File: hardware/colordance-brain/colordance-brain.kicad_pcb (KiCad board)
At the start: 2 copper layers, 129.5 x 83.5 mm, 118 parts, among them J1 Anderson, J10 RJ45, J11 RJ45, J12 RJ45, J13 RJ45, J14 RJ45, J2 Conn_01x06, J3 Conn_01x03, J4 Conn_01x03, J5 Conn_01x03, J6 Conn_01x03, J7 Conn_01x06, J8 Conn_01x05, J9 RJ45, U1 AP3211, U2 Teensy4.1, U3 AM26LS31x, U4 AM26LS31x, U5 AM26LS31x, U6 74AHCT1G126, U7 74AHCT1G126

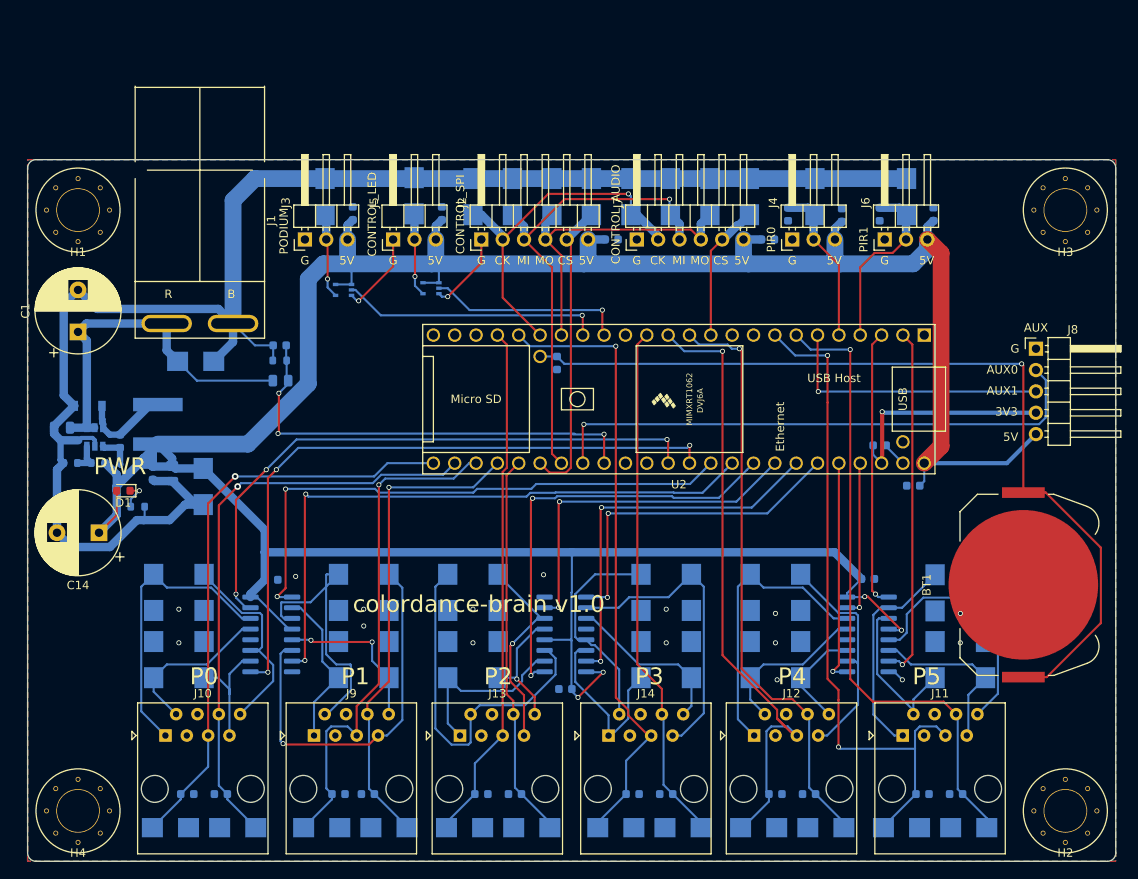
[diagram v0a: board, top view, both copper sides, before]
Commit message: Convert colordance-brain to KiCAD 6
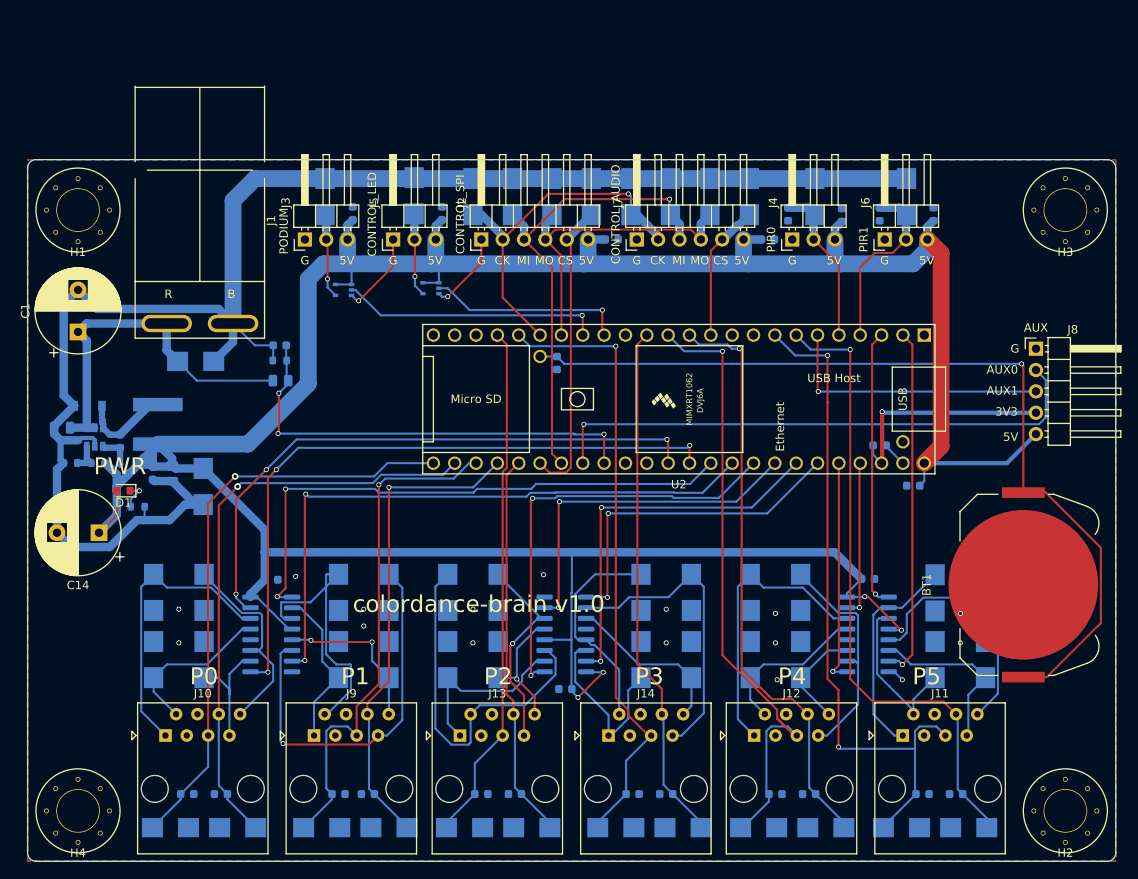
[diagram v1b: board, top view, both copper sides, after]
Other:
- net class Default removed

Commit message: colordance-brain v1.1
- Switch from SPI to serial-over-RS422 for communication with the
interface. Using the Teensy 4.1 as a SPI peripheral did not work. Using
RS422 will allow us to place the interface far away (e.g. 50ft) from the
brain.
- Also break out an extra serial port, e.g. for music playing?
- Change protection for most I/O pins to resistor + cap instead of TVS
diode
- Add a builtin button, for activating test modes
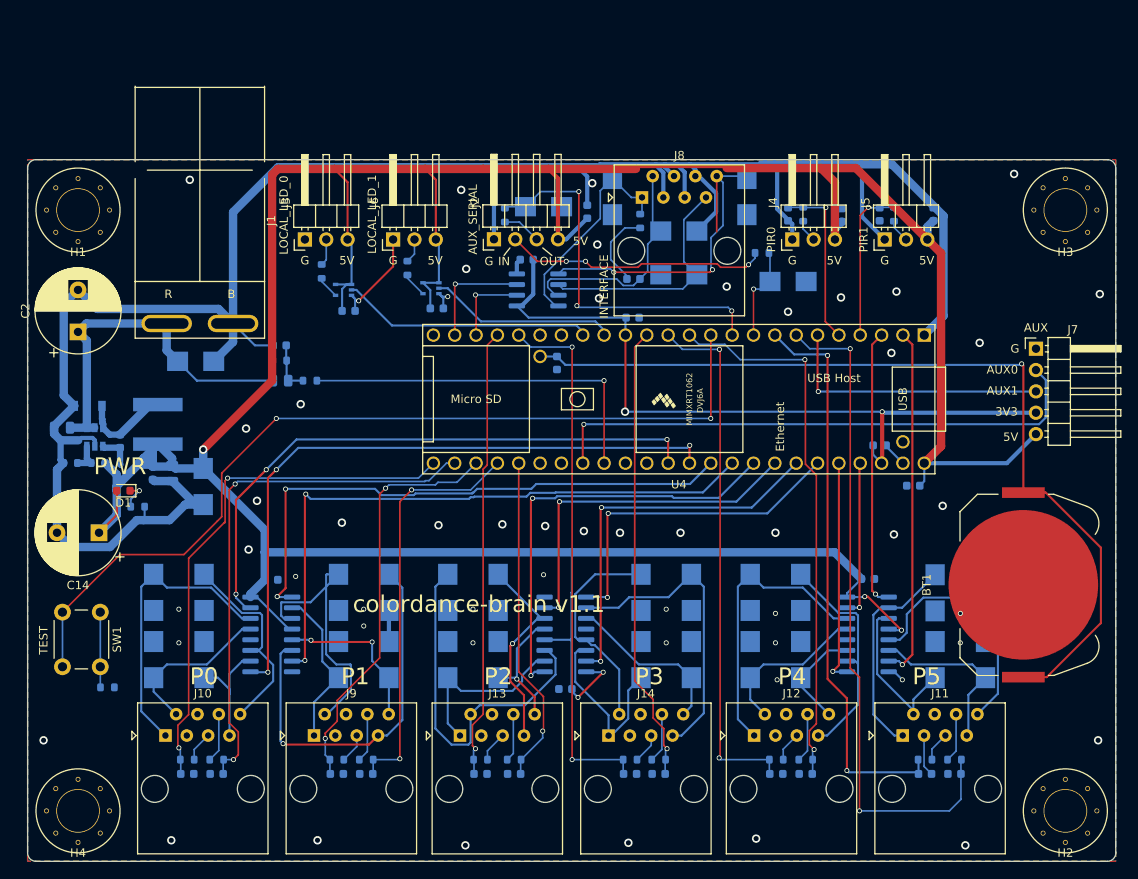
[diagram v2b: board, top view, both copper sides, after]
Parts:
- removed the C13 at (103.1, 56.0)
- removed the C21 at (38.0, 122.0)
- removed the C22 at (34.0, 122.0)
- removed the C26 at (108.0, 122.0)
- removed the C27 at (104.0, 122.0)
- removed the C31 at (91.0, 122.0)
- removed the C32 at (87.0, 122.0)
- removed the C4 at (84.5, 56.0)
- removed the D12 at (119.6, 50.9)
- removed the D13 at (68.0, 50.9)
- removed the D15 at (91.5, 50.9)
- removed the D16 at (77.4, 50.9)
- removed the D17 at (100.9, 50.9)
- removed the D18 at (58.0, 126.0)
- removed the D19 at (50.0, 126.0)
- removed the D24 at (40.0, 126.0)
- removed the D25 at (32.0, 126.0)
- removed the D30 at (127.0, 126.0)
- removed the D31 at (119.0, 126.0)
- removed D36, D37, D42, D43, D48, D49: D_TVS_5V, Diode_SMD:D_SMB
- removed the D5 at (108.7, 50.9)
- removed the D6 at (72.7, 50.9)
- removed the D7 at (96.2, 50.9)
- removed the J7 at (87.5, 56.0)
- added C1: 0.1uF, Capacitor_SMD:C_0603_1608Metric, B.Cu at (81.6, 52.7)
- added C15: 0.1uF, Capacitor_SMD:C_0603_1608Metric, B.Cu at (87.0, 65.3)
- added C19: 0.1uF, Capacitor_SMD:C_0603_1608Metric, B.Cu at (74.4, 58.4)
- added C20: 1300pF, Capacitor_SMD:C_0603_1608Metric, B.Cu at (87.1, 60.7)
- added C24: 22nF, Capacitor_SMD:C_0603_1608Metric, B.Cu at (37.5, 119.6)
- added C25: 22nF, Capacitor_SMD:C_0603_1608Metric, B.Cu at (34.0, 119.6)
- added C29: 22nF, Capacitor_SMD:C_0603_1608Metric, B.Cu at (107.6, 119.6)
- added C30: 22nF, Capacitor_SMD:C_0603_1608Metric, B.Cu at (104.1, 119.6)
- added C34: 22nF, Capacitor_SMD:C_0603_1608Metric, B.Cu at (90.1, 119.6)
- added C35: 22nF, Capacitor_SMD:C_0603_1608Metric, B.Cu at (86.7, 119.6)
- added D11: D_TVS_DATA, Diode_SMD:D_SMB, B.Cu at (100.6, 50.9)
- added D9: D_TVS_DATA, Diode_SMD:D_SMB, B.Cu at (92.5, 55.0)
- added J8: RJ45, Connector_RJ:RJ45_Amphenol_54602-x08_Horizontal, F.Cu at (88.1, 51.0)
- added R12: 1k, Resistor_SMD:R_0603_1608Metric, B.Cu at (118.1, 53.0)
- added R13: 100, Resistor_SMD:R_0603_1608Metric, B.Cu at (60.2, 59.4)
- added R14: 120, Resistor_SMD:R_0603_1608Metric, B.Cu at (87.9, 53.8)
- added R15: 1k, Resistor_SMD:R_0603_1608Metric, B.Cu at (55.3, 117.9)
- added R16: 1k, Resistor_SMD:R_0603_1608Metric, B.Cu at (51.8, 117.9)
- added R17: 1k, Resistor_SMD:R_0603_1608Metric, B.Cu at (37.5, 117.9)
- added R18: 1k, Resistor_SMD:R_0603_1608Metric, B.Cu at (34.0, 117.9)
- added R19: 1k, Resistor_SMD:R_0603_1608Metric, B.Cu at (125.3, 117.9)
- added R20: 1k, Resistor_SMD:R_0603_1608Metric, B.Cu at (121.8, 117.9)
- added R21: 1k, Resistor_SMD:R_0603_1608Metric, B.Cu at (107.6, 117.9)
- added R22: 1k, Resistor_SMD:R_0603_1608Metric, B.Cu at (104.1, 117.9)
- added R23: 1k, Resistor_SMD:R_0603_1608Metric, B.Cu at (72.9, 117.9)
- added R24: 1k, Resistor_SMD:R_0603_1608Metric, B.Cu at (68.9, 117.9)
- added R25: 1k, Resistor_SMD:R_0603_1608Metric, B.Cu at (90.1, 117.9)
- added R26: 1k, Resistor_SMD:R_0603_1608Metric, B.Cu at (86.7, 117.9)
- added R4: 100, Resistor_SMD:R_0603_1608Metric, B.Cu at (102.4, 57.6)
- added R5: 100, Resistor_SMD:R_0603_1608Metric, B.Cu at (50.0, 59.8)
- added R6: 1k, Resistor_SMD:R_0603_1608Metric, B.Cu at (107.3, 53.0)
- added R7: 1k, Resistor_SMD:R_0603_1608Metric, B.Cu at (48.6, 72.8)
- added R8: 100, Resistor_SMD:R_0603_1608Metric, B.Cu at (71.8, 53.1)
- added R9: 1k, Resistor_SMD:R_0603_1608Metric, B.Cu at (24.5, 109.3)
- added SW1: SW_SPST, Button_Switch_THT:SW_PUSH_6mm, F.Cu at (23.6, 100.3)
- added U5: ISL83490, Package_SO:SOIC-8_3.9x4.9mm_P1.27mm, B.Cu at (75.7, 62.0)
- C10: renamed from C11; value 0.1uF -> 22nF
- C22: renamed from C19; value 0.1uF -> 22nF
- C23: renamed from C20; value 0.1uF -> 22nF
- C27: renamed from C24; value 0.1uF -> 22nF
- C28: renamed from C25; value 0.1uF -> 22nF
- C32: renamed from C29; value 0.1uF -> 22nF
- C33: renamed from C30; value 0.1uF -> 22nF
- C6: value 0.1uF -> 22nF
- D10, D8: value D_TVS_5V -> D_TVS_DATA
- J2: value Conn_01x06 -> Conn_01x04; footprint Connector_PinHeader_2.54mm:PinHeader_1x06_P2.54mm_Horizontal -> Connector_PinHeader_2.54mm:PinHeader_1x04_P2.54mm_Horizontal
- moved D10 32.9 mm to (92.5, 60.2), turned to 180 degrees
- moved D4 26.0 mm to (76.4, 52.1), turned to 180 degrees
- moved D3 21.3 mm to (105.5, 61.0), turned to 180 degrees
- moved C3 11.6 mm to (53.2, 64.5), turned to 0 degrees
- moved C13 11.3 mm to (63.7, 64.2), turned to 0 degrees
- moved D8 2.50 mm to (84.6, 50.9), turned to -90 degrees
- moved C28 2.42 mm to (121.8, 119.6)
- moved C22 2.41 mm to (55.3, 119.6)
- moved C23 2.41 mm to (51.8, 119.6)
- moved C27 2.41 mm to (125.3, 119.6)
- moved C32 2.40 mm to (72.9, 119.6)
- moved C33 2.40 mm to (68.9, 119.6)
- moved J2 1.50 mm to (70.5, 56.0)
- renumbered C10 to C11, C8 to C13, C15 to C16, C16 to C17, C17 to C18, C1 to C2, C18 to C21, C23 to C26, C2 to C3, C28 to C31, C3 to C4, C33 to C7, C7 to C8, D20 to D12, D21 to D13, D22 to D14, D23 to D15, D26 to D16, D27 to D17, D28 to D18, D29 to D19, D32 to D20, D33 to D21, D34 to D22, D35 to D23, D38 to D24, D39 to D25, D40 to D26, D41 to D27, D44 to D28, D45 to D29, D46 to D30, D47 to D31, D50 to D32, D51 to D33, D52 to D34, D53 to D35, D9 to D5, D11 to D6, D14 to D7, J6 to J5, J5 to J6, J8 to J7, R4 to R10, R5 to R11, U6 to U1, U1 to U2, U7 to U3, U2 to U4, U3 to U6, U4 to U7, U5 to U8
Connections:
- net CONTROL_PANEL_LED renamed LOCAL_LED_1
- net PODIUM_LED renamed LOCAL_LED_0
- C7 pad 1: BATT_DIV -> Net-(C7-Pad1)
- D10 pad 1: Net-(D10-Pad1) -> /INTERFACE_Z
- D3 pad 1: SCK -> GND
- D3 pad 2: GND -> /AUX_SERIAL_IN
- D4 pad 1: Net-(D4-Pad1) -> GND
- D4 pad 2: GND -> /AUX_SERIAL_OUT
- D8 pad 1: CS_CTRL -> /INTERFACE_A
- J10 pad 5: POLE0_PIR1 -> Net-(J10-Pad5)
- J10 pad 6: POLE0_PIR0 -> Net-(J10-Pad6)
- J11 pad 5: POLE5_PIR1 -> Net-(J11-Pad5)
- J11 pad 6: POLE5_PIR0 -> Net-(J11-Pad6)
- J12 pad 5: POLE4_PIR1 -> Net-(J12-Pad5)
- J12 pad 6: POLE4_PIR0 -> Net-(J12-Pad6)
- J13 pad 5: POLE2_PIR1 -> Net-(J13-Pad5)
- J13 pad 6: POLE2_PIR0 -> Net-(J13-Pad6)
- J14 pad 5: POLE3_PIR1 -> Net-(J14-Pad5)
- J14 pad 6: POLE3_PIR0 -> Net-(J14-Pad6)
- J2 pad 2: SCK -> Net-(J2-Pad2)
- J2 pad 3: MISO -> Net-(J2-Pad3)
- J2 pad 4: MOSI -> +5V
- J3 pad 2: Net-(D4-Pad1) -> Net-(J3-Pad2)
- J4 pad 2: LOCAL_PIR0 -> Net-(J4-Pad2)
- J5 pad 2: LOCAL_PIR1 -> Net-(J5-Pad2)
- J6 pad 2: Net-(D10-Pad1) -> Net-(J6-Pad2)
- J9 pad 5: POLE1_PIR1 -> Net-(J9-Pad5)
- J9 pad 6: POLE1_PIR0 -> Net-(J9-Pad6)
- R2 pad 2: BATT_DIV -> Net-(C7-Pad1)
- R3 pad 1: BATT_DIV -> Net-(C7-Pad1)
- U1 pad 4: Net-(D4-Pad1) -> Net-(R5-Pad1)
- U3 pad 4: Net-(D10-Pad1) -> Net-(R13-Pad1)
- U4 pad 10: (no net) -> /AUX_SERIAL_OUT
- U4 pad 11: CS_AUDIO -> /SW_BUILTIN
- U4 pad 15: (no net) -> +3V3
- U4 pad 18: MOSI -> unconnected-(U4-Pad18)
- U4 pad 19: SCK -> unconnected-(U4-Pad19)
- U4 pad 22: (no net) -> /INTERFACE_IN
- U4 pad 23: (no net) -> /INTERFACE_OUT
- U4 pad 24: (no net) -> unconnected-(U4-Pad24)
- U4 pad 30: CS_CTRL -> unconnected-(U4-Pad30)
- U4 pad 31: MISO -> unconnected-(U4-Pad31)
- U4 pad 34: (no net) -> unconnected-(U4-Pad34)
- U4 pad 35: (no net) -> unconnected-(U4-Pad35)
- U4 pad 49: (no net) -> unconnected-(U4-Pad49)
- U4 pad 9: (no net) -> /AUX_SERIAL_IN
- U6 pad 12: (no net) -> unconnected-(U6-Pad12)
- U7 pad 12: (no net) -> unconnected-(U7-Pad12)
- U8 pad 12: (no net) -> unconnected-(U8-Pad12)
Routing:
- net /SW_BUILTIN: track 0.00 -> 106.2 mm, vias 0 -> 2
- net GND: track 219.8 -> 303.4 mm, vias 18 -> 54
- net +3V3: track 27.0 -> 89.1 mm, vias 1 -> 2
- net MISO: track 56.6 -> 0.00 mm, vias 1 -> 0
- net /AUX_SERIAL_OUT: track 0.00 -> 44.9 mm, vias 0 -> 3
- net SCK: track 42.7 -> 0.00 mm, vias 1 -> 0
- net /INTERFACE_Y: track 0.00 -> 41.3 mm, vias 0 -> 2
- net +5V: track 370.4 -> 409.9 mm, vias 4 -> 5
- net MOSI: track 38.3 -> 0.00 mm
- net CS_CTRL: track 35.9 -> 0.00 mm
- net Net-(J2-Pad2): track 0.00 -> 31.3 mm, vias 0 -> 3
- net /INTERFACE_Z: track 0.00 -> 28.3 mm
- net /INTERFACE_B: track 0.00 -> 27.7 mm
- net /INTERFACE_A: track 0.00 -> 25.9 mm
- net CS_AUDIO: track 16.4 -> 0.00 mm
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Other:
- board text added: "A"
- board text added: "AUX_SERIAL"
- board text added: "B"
- board text added: "IN"
- board text added: "INTERFACE"
- board text added: "LOCAL_LED_0"
- board text added: "LOCAL_LED_1"
- board text added: "OUT"
- board text added: "TEST"
- board text added: "Y"
- board text added: "Z"
- board text added: "colordance-brain v1.1"
- board text removed: "CK"
- board text removed: "CONTROL_AUDIO"
- board text removed: "CONTROL_LED"
- board text removed: "CONTROL_SPI"
- board text removed: "CS"
- board text removed: "MI"
- board text removed: "MO"
- board text removed: "PODIUM"
- board text removed: "colordance-brain v1.0"

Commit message: Start updating brain for v1.2
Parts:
- removed the C11 at (32.2, 83.8)
- removed the C12 at (29.9, 83.8)
- removed the C14 at (23.5, 90.9)
- removed the C2 at (21.0, 67.0)
- removed the C5 at (19.1, 78.4)
- removed the C8 at (26.0, 80.0)
- removed the D2 at (35.0, 70.5)
- removed the D5 at (22.2, 75.8)
- removed the D6 at (27.1, 82.8)
- removed the D7 at (35.9, 85.4)
- removed the J1 at (35.5, 66.0)
- removed the R10 at (23.4, 82.6)
- removed the R11 at (20.1, 82.6)
- removed the U2 at (23.0, 79.5)
- added C30: 470uF, Capacitor_THT:CP_Radial_D10.0mm_P5.00mm, F.Cu at (21.2, 67.0)
- added C31: 22uF, Capacitor_SMD:C_0805_2012Metric, B.Cu at (19.1, 78.4)
- added C32: 10nF, Capacitor_SMD:C_0603_1608Metric, B.Cu at (25.9, 80.0)
- added C33: 22uF, Capacitor_SMD:C_0805_2012Metric, B.Cu at (32.2, 83.8)
- added C34: 0.1uF, Capacitor_SMD:C_0603_1608Metric, B.Cu at (30.0, 83.8)
- added C35: 470uF, Capacitor_THT:CP_Radial_D10.0mm_P5.00mm, F.Cu at (23.5, 90.5)
- added C36: 0.1uF, Capacitor_SMD:C_0603_1608Metric, B.Cu at (131.2, 53.2)
- added C37: 22nF, Capacitor_SMD:C_0603_1608Metric, B.Cu at (126.2, 52.8)
- added C38: 470uF, Capacitor_THT:CP_Radial_D10.0mm_P5.00mm, F.Cu at (117.9, 90.0)
- added D32: D_TVS_12V, Diode_SMD:D_SMB, B.Cu at (35.5, 70.6)
- added D33: SCHOTTKY, Diode_SMD:D_SOD-123, B.Cu at (22.2, 75.9)
- added D34: D, Diode_SMD:D_SOD-323, B.Cu at (27.1, 82.7)
- added D35: D_TVS_5V, Diode_SMD:D_SMB, B.Cu at (35.8, 85.4)
- added J14: Anderson, Homebrew:Anderson_1336G1_right_angle_bottom_two, F.Cu at (35.6, 66.4)
- added J15: Conn_01x03, Connector_PinHeader_2.54mm:PinHeader_1x03_P2.54mm_Horizontal, F.Cu at (126.2, 56.0)
- added R25: 11.5k, Resistor_SMD:R_0603_1608Metric, B.Cu at (23.4, 82.6)
- added R26: 2.21k, Resistor_SMD:R_0603_1608Metric, B.Cu at (20.2, 82.6)
- added R27: 1k, Resistor_SMD:R_0603_1608Metric, B.Cu at (127.9, 52.8)
- added U8: AP3211, Package_TO_SOT_SMD:SOT-23-6, B.Cu at (23.0, 79.5)
- H1, H2, H3, H4: footprint homebrew:HOLE_5MM_#8 -> Homebrew:HOLE_5MM_#8
- U3: renamed from U4; footprint homebrew:Teensy41_stripped -> Homebrew:Teensy41_stripped
- moved C14 29.1 mm to (110.0, 42.7)
- moved D4 29.1 mm to (107.5, 32.9)
- moved R12 29.1 mm to (110.8, 35.8)
- moved J7 13.2 mm to (96.9, 60.9), turned to 180 degrees
- moved D7 11.9 mm to (94.7, 40.6), turned to 0 degrees
- moved D6 2.80 mm to (92.4, 57.4), turned to 0 degrees
- moved D5 2.40 mm to (92.4, 52.6)
- moved C7 0.88 mm to (115.5, 53.0)
- moved C3 0.88 mm to (121.9, 53.0)
- moved J4 0.88 mm to (116.1, 56.0)
- moved R10 0.88 mm to (117.2, 53.0)
- moved L1 0.10 mm to (30.5, 77.9)
- renumbered C16 to C10, C17 to C11, C18 to C12, C19 to C13, C20 to C14, C21 to C15, C22 to C16, C23 to C17, C24 to C18, C25 to C19, C3 to C2, C26 to C20, C27 to C21, C28 to C22, C29 to C23, C30 to C24, C31 to C25, C32 to C26, C33 to C27, C34 to C28, C35 to C29, C4 to C3, C6 to C4, C7 to C5, C9 to C6, C10 to C7, C13 to C8, C15 to C9, D14 to D10, D15 to D11, D16 to D12, D17 to D13, D18 to D14, D19 to D15, D20 to D16, D21 to D17, D22 to D18, D23 to D19, D3 to D2, D24 to D20, D25 to D21, D26 to D22, D27 to D23, D28 to D24, D29 to D25, D30 to D26, D31 to D27, D32 to D28, D33 to D29, D4 to D3, D34 to D30, D35 to D31, D8 to D4, D9 to D5, D10 to D6, D11 to D7, D12 to D8, D13 to D9, J2 to J1, J11 to J10, J12 to J11, J13 to J12, J14 to J13, J3 to J2, J4 to J3, J5 to J4, J6 to J5, J7 to J6, J8 to J7, J9 to J8, J10 to J9, R12 to R10, R13 to R11, R14 to R12, R15 to R13, R16 to R14, R17 to R15, R18 to R16, R19 to R17, R20 to R18, R21 to R19, R22 to R20, R23 to R21, R24 to R22, R25 to R23, R26 to R24, U3 to U2, U5 to U4, U6 to U5, U7 to U6, U8 to U7
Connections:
- U3 pad 16: LOCAL_LED_1 -> /INTERFACE_OUT
- U3 pad 17: LOCAL_LED_0 -> /INTERFACE_IN
- U3 pad 19: unconnected-(U4-Pad19) -> LOCAL_PIR2
- U3 pad 22: /INTERFACE_IN -> LOCAL_LED_1
- U3 pad 23: /INTERFACE_OUT -> LOCAL_LED_0
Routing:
- net LOCAL_PIR2: track 0.00 -> 76.0 mm, vias 0 -> 3
- net /INTERFACE_Y: track 41.3 -> 0.00 mm, vias 2 -> 0
- net /INTERFACE_Z: track 28.3 -> 0.00 mm
- net /INTERFACE_B: track 27.7 -> 0.00 mm
- net GND: track 303.4 -> 275.7 mm, vias 54 -> 49
- net /INTERFACE_A: track 25.9 -> 0.00 mm
- net +5V: track 409.9 -> 427.5 mm, vias 5 -> 6
- net LOCAL_LED_0: track 30.0 -> 15.2 mm, vias 0 -> 1
- net LOCAL_LED_1: track 22.3 -> 9.84 mm, vias 0 -> 1
- net Net-(C14-Pad1): track 9.39 -> 0.00 mm
- net +3V3: track 89.1 -> 97.1 mm
- net /INTERFACE_IN: track 9.75 -> 17.3 mm, vias 1 -> 2
- net /INTERFACE_OUT: track 13.5 -> 19.0 mm, vias 1 -> 2
- net Net-(C8-Pad1): track 4.17 -> 0.00 mm
- net Net-(C32-Pad1): track 0.00 -> 4.17 mm
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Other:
- board text added: "colordance-brain v1.2"
- board text removed: "colordance-brain v1.1"

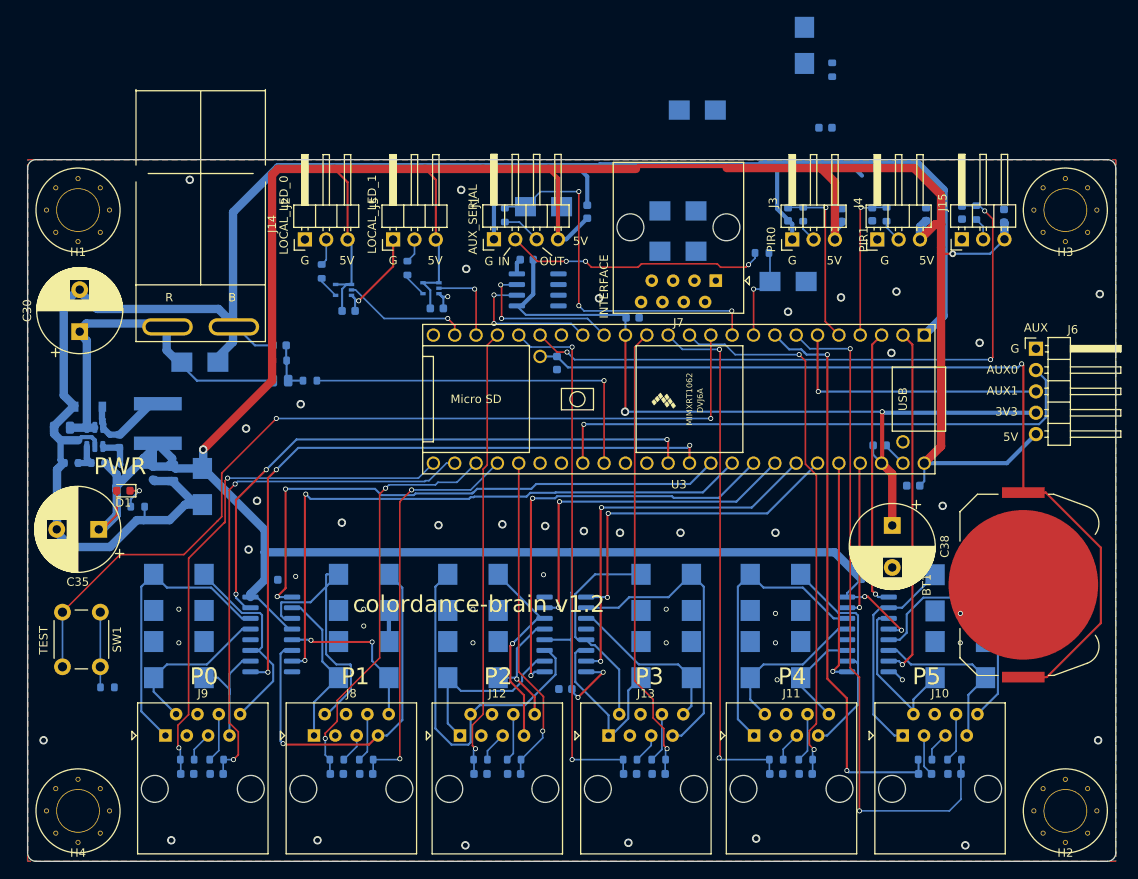
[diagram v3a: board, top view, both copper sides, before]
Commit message: colordance-brain hardware v1.2:
- Fix interface RJ45 port orientation
- Add a third local PIR port
- Fix interface to use a serial port, not a CAN port
- Add a 470uF cap for the 3v3 rail
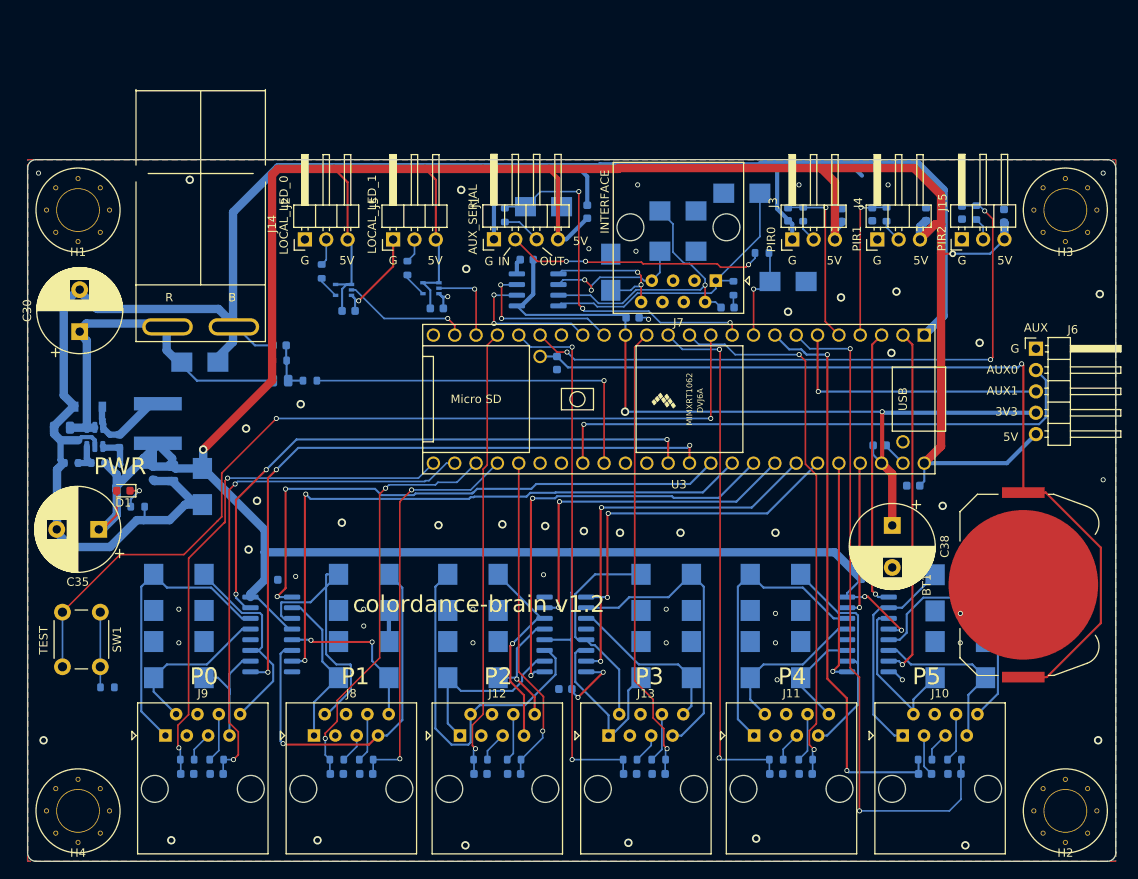
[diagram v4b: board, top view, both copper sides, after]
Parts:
- moved R12 28.5 mm to (99.0, 61.8)
- moved C14 24.4 mm to (98.3, 64.1), turned to 180 degrees
- moved D7 21.9 mm to (84.4, 59.9), turned to -90 degrees
- moved D4 19.1 mm to (100.0, 50.5), turned to 180 degrees
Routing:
- net /INTERFACE_A: track 0.00 -> 35.6 mm
- net /INTERFACE_B: track 0.00 -> 34.4 mm, vias 0 -> 1
- net /INTERFACE_Y: track 0.00 -> 17.3 mm, vias 0 -> 2
- net /INTERFACE_Z: track 0.00 -> 17.1 mm, vias 0 -> 2
- net Net-(C14-Pad1): track 0.00 -> 1.51 mm
- net GND: track 275.7 -> 276.8 mm, vias 49 -> 57
- net /AUX_SERIAL_OUT: track 44.6 -> 43.7 mm
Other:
- board text added: "PIR2"
